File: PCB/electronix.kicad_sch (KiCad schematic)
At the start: 96 parts, among them IC1 ICM-20602, IC2 AP9101CK6-ANTRG1, IC3 DRV8210DRLR, IC4 DRV8210DRLR, J1 USB-C 6pin, J2 PRG, M1 N20 motor, M2 N20 motor, Q1 UMH3N FHA, Q2 757-SSM6N7002KFULF, Q3 757-SSM6N7002KFULF, Q4 Phototransistor, Q5 Phototransistor, Q6 757-SSM6N7002KFULF, Q7 Phototransistor, Q8 Phototransistor, SW1 SW_DIP_x01, SW2 RESET, SW3 START, U1 MCP73213-A6SI/MF, U2 ESP32-WROOM-32, U3 LMR51420YDDRCR

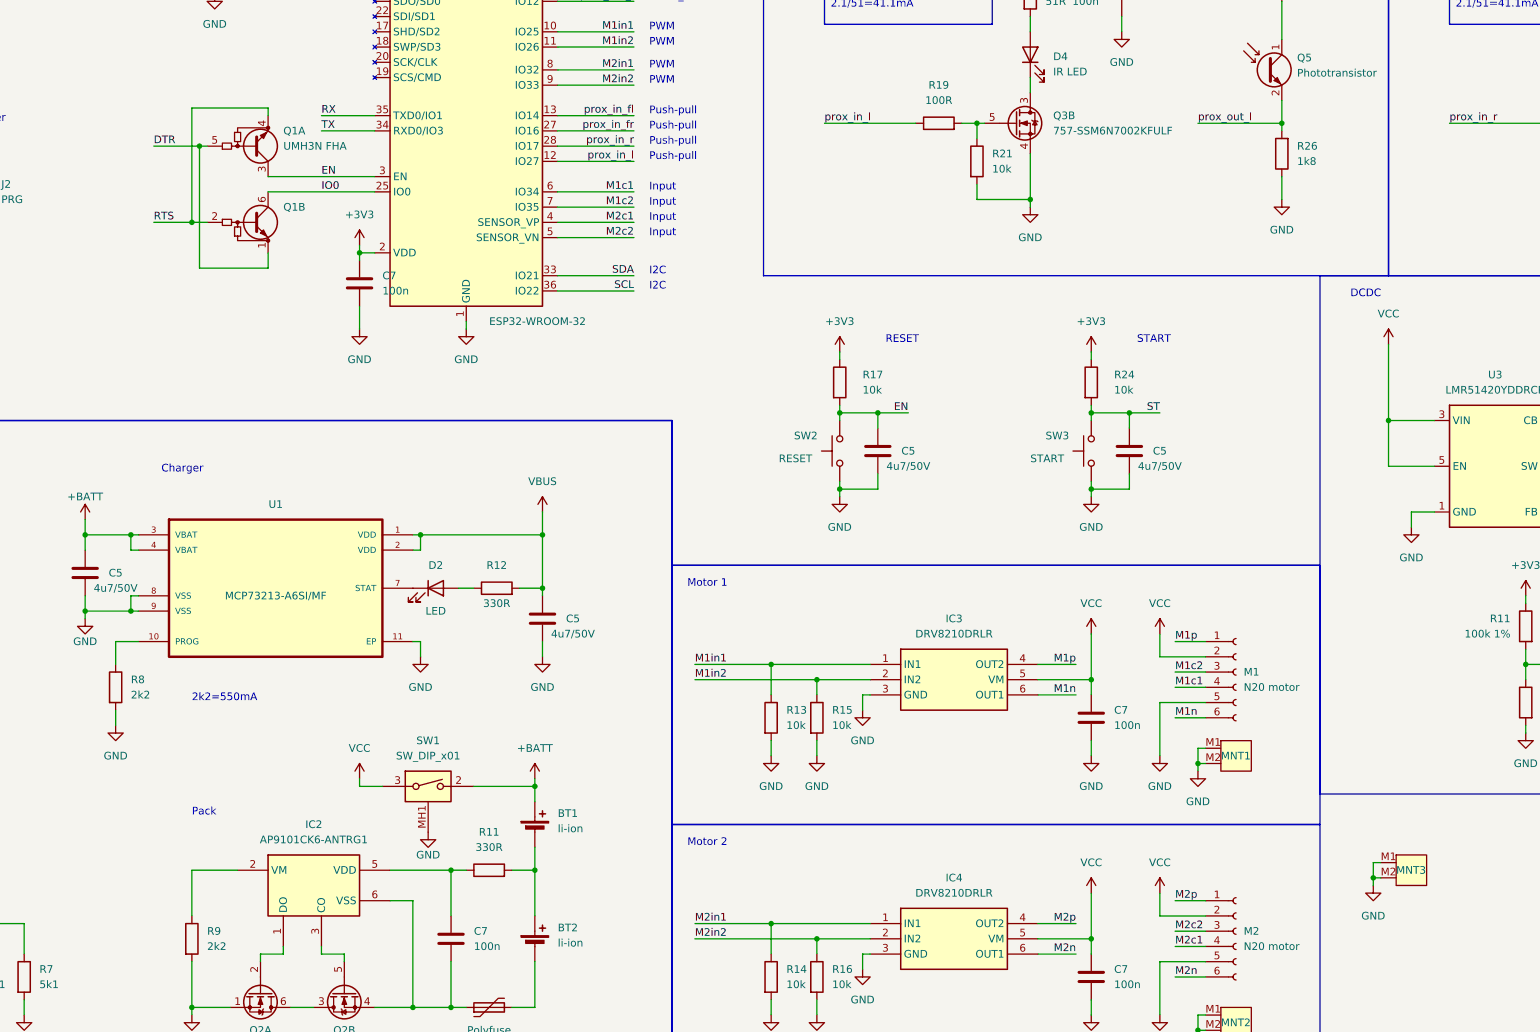
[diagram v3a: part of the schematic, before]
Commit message: add bigger ESP32 bypass
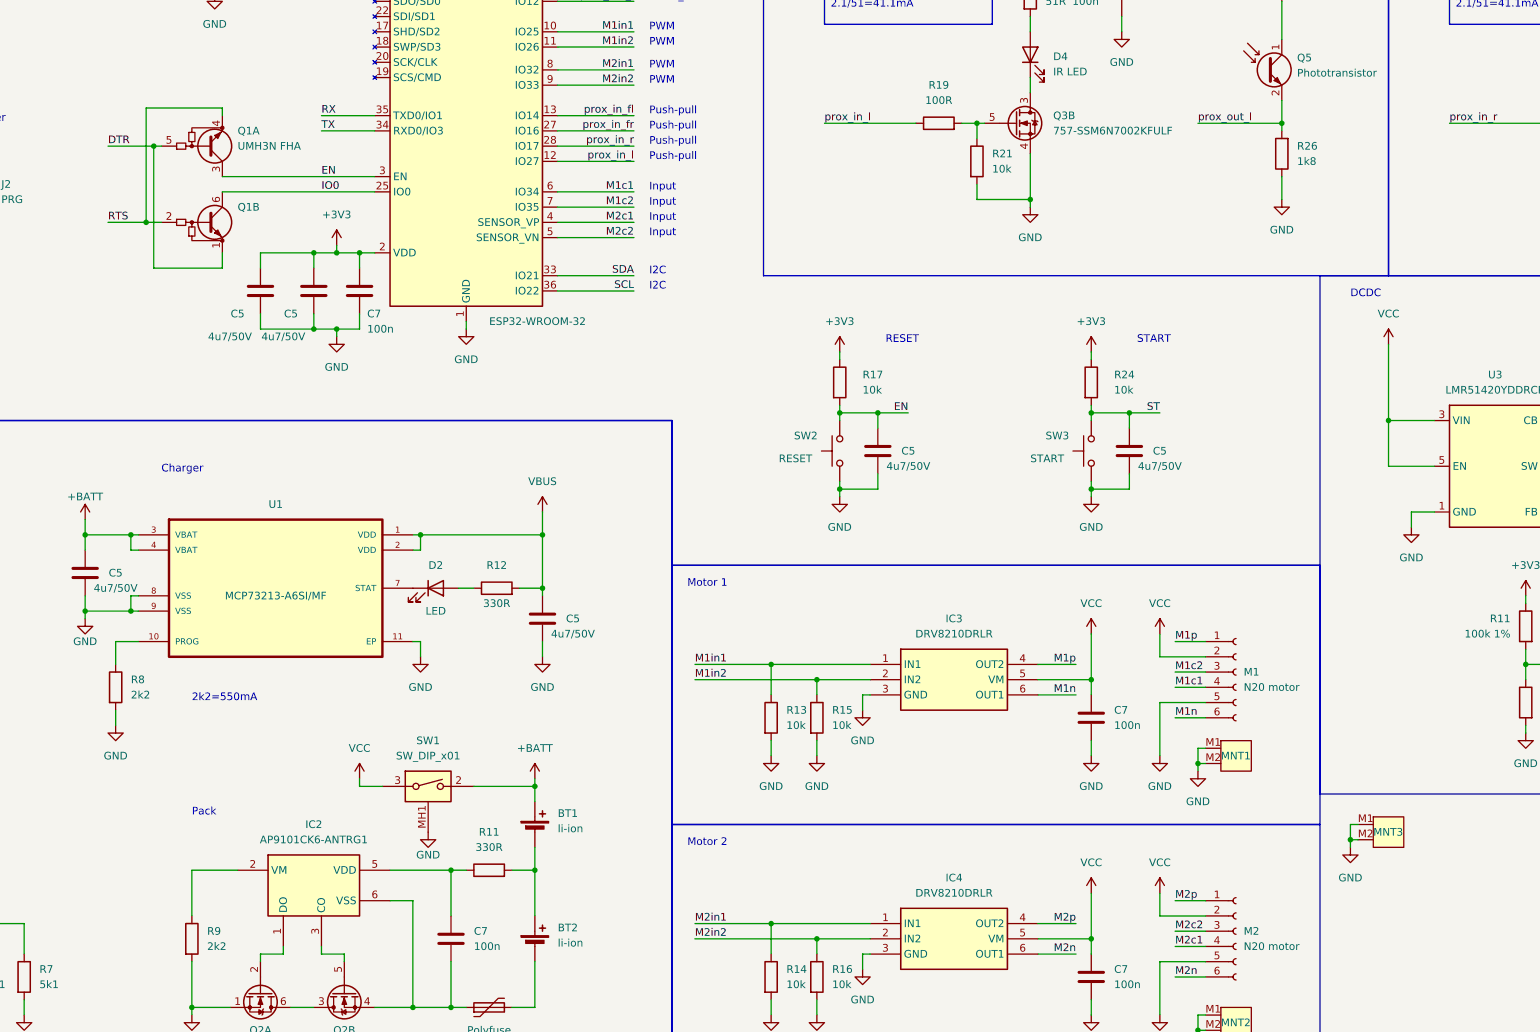
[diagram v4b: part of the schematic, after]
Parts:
- added C5 (x2): 4u7/50V, Capacitor_SMD:C_0805_2012Metric, symbol Device:C
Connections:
- net +3V3: now also C5.1, C5.1
- net GND: now also C5.2, C5.2
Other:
- moved on the sheet: C7, MNT3, Q1A, Q1B

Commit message: Add power source switching Add Mouser PN to parts to enable BOM generation Moved PWR indicator to side of board
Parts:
- removed D1: D, Diode_SMD:D_SOD-128, symbol Device:D
- removed D8: LED, LED_SMD:LED_0603_1608Metric, symbol Device:LED
- removed R37: 330R, Resistor_SMD:R_0603_1608Metric, symbol Device:R
- added D5: LED, LED_SMD:LED_0603_1608Metric, symbol Device:LED
- added IC5: LM66200DRLR, Package_TO_SOT_SMD:SOT-583-8, symbol LM66200DRLR:LM66200DRLR
- added R15: 10k, Resistor_SMD:R_0603_1608Metric, symbol Device:R
- added R26: 330R, Resistor_SMD:R_0603_1608Metric, symbol Device:R
- C5: Mouser Part Number (none) -> 81-GRM21BZ71H475ME5K
- C7: Mouser Part Number (none) -> 187-CL10B104KB8NNNC
- C7: value 100n/50V -> 100n; Mouser Part Number (none) -> 187-CL10B104KB8NNNC
- D1, D2: Mouser Part Number (none) -> 710-150060AS75000
- F1: Mouser Part Number (none) -> 576-1812L150/16DR
- IC1: Manufacturer_Name TDK -> (none); Manufacturer_Part_Number ICM-20602 -> (none); Mouser Price/Stock https://www.mouser.co.uk/ProductDetail/TDK-InvenSense/ICM-2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 -> (none)
- IC2: Height 1.4 -> (none); Manufacturer_Name Diodes Inc. -> (none); Manufacturer_Part_Number AP9101CK6-ANTRG1 -> (none); Mouser Price/Stock https://www.mouser.co.uk/ProductDetail/Diodes-Incorporated/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 -> (none)
- IC3, IC4: Height 0.6 -> (none); Manufacturer_Name Texas Instruments -> (none); Manufacturer_Part_Number DRV8210DRLR -> (none); Mouser Price/Stock https://www.mouser.co.uk/ProductDetail/Texas-Instruments/DR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 -> (none)
- J1: Mouser Part Number (none) -> 649-10164359-00011LF
- J2: Mouser Part Number (none) -> 992-6FX1L-254MM
- L1: Mouser Part Number (none) -> 963-NRS5040T3R3NMGJ
- Q1: Mouser Part Number (none) -> 755-UMH3NFHATN
- Q2, Q3, Q6: value 757-SSM6N7002KFULF -> dual NMOS; Mouser Part Number (none) -> 757-SSM6N7002KFULF
- R1, R4, R5: Mouser Part Number (none) -> 667-ERJ-3EKF1002V
- R10: Mouser Part Number (none) -> 791-RMC1/16-331JTP
- R11: Mouser Part Number (none) -> 603-RC0603FR-10100KL
- R11: renamed from R17; Mouser Part Number (none) -> 667-ERJ-3EKF1002V
- R12: renamed from R11; Mouser Part Number (none) -> 791-RMC1/16-331JTP
- R12: Mouser Part Number (none) -> 708-RMCF0603FT22K1
- R13: renamed from R12; Mouser Part Number (none) -> 791-RMC1/16-331JTP
- R14: renamed from R24; Mouser Part Number (none) -> 667-ERJ-3EKF1002V
- R16: renamed from R13; Mouser Part Number (none) -> 667-ERJ-3EKF1002V
- R17: renamed from R14; Mouser Part Number (none) -> 667-ERJ-3EKF1002V
- R18: renamed from R15; Mouser Part Number (none) -> 667-ERJ-3EKF1002V
- R19: renamed from R16; Mouser Part Number (none) -> 667-ERJ-3EKF1002V
- R20: renamed from R18; Mouser Part Number (none) -> 756-WCR0603-100RFI
- R21: renamed from R19; Mouser Part Number (none) -> 756-WCR0603-100RFI
- R22: renamed from R20; Mouser Part Number (none) -> 667-ERJ-3EKF1002V
- R23: renamed from R21; Mouser Part Number (none) -> 667-ERJ-3EKF1002V
- R24: renamed from R22; Mouser Part Number (none) -> 667-ERJ-PA3J510V
- R25: renamed from R23; Mouser Part Number (none) -> 667-ERJ-PA3J510V
- R27: renamed from R25; Mouser Part Number (none) -> 603-RC0603JR-071K8L
- R28: renamed from R26; Mouser Part Number (none) -> 603-RC0603JR-071K8L
- R31: renamed from R29; Mouser Part Number (none) -> 756-WCR0603-100RFI
- R32: renamed from R30; Mouser Part Number (none) -> 756-WCR0603-100RFI
- R33: renamed from R31; Mouser Part Number (none) -> 667-ERJ-3EKF1002V
- R34: renamed from R32; Mouser Part Number (none) -> 667-ERJ-3EKF1002V
- R35: renamed from R33; Mouser Part Number (none) -> 667-ERJ-PA3J510V
- R36: renamed from R34; Mouser Part Number (none) -> 667-ERJ-PA3J510V
- R37: renamed from R35; Mouser Part Number (none) -> 603-RC0603JR-071K8L
- R38: renamed from R36; Mouser Part Number (none) -> 603-RC0603JR-071K8L
- R6, R7: Mouser Part Number (none) -> 301-5.1K-RC
- R8, R9: Mouser Part Number (none) -> 660-RK73B1JTTD222J
- SW1: value SW_DIP_x01 -> side slide; Mouser Part Number (none) -> 655-1825232-1
- SW2, SW3: Mouser Part Number (none) -> 611-PTS636SL50LFS
- U1: AVAILABILITY Good -> (none); DESCRIPTION MCP Series 16V Dual-Cell Li-Ion/Li-Polymer Battery Charge M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 -> (none); MF Microchip -> (none); MP MCP73213-A6SI/MF -> (none); Mouser Part Number (none) -> 579-MCP73213-A6SI/MF; PACKAGE DFN-10 Microchip -> (none); PRICE 1.60 USD -> (none); SNAPEDA_PACKAGE_ID 30778 -> (none)
- U2: Mouser Part Number (none) -> 356-ESP32WRM32E132PH
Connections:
- net +3V3: now also D5.2 (A), IC5.2 (VOUT), IC5.7 (VOUT); no longer C5.1, C5.1, C5.1, L1.2, R11.1
- net GND: now also IC5.1 (GND), IC5.4 (~{ON}), IC5.5 (GND), R26.1
- net 3V3_PRG: now reaches J2.6 (Pin_6)
- net 3V3_PRG: now also IC5.6 (VIN2)
- new net: D5.1 (K), R26.2
- new net: IC5.8 (ST), R15.2
- new net 3V3_SW: C5.1, C5.1, C5.1, IC5.3 (VIN1), L1.2, R11.1, R15.1
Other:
- note added: "Power Switching"
- moved on the sheet: C5, R11, R14, SW2, SW3

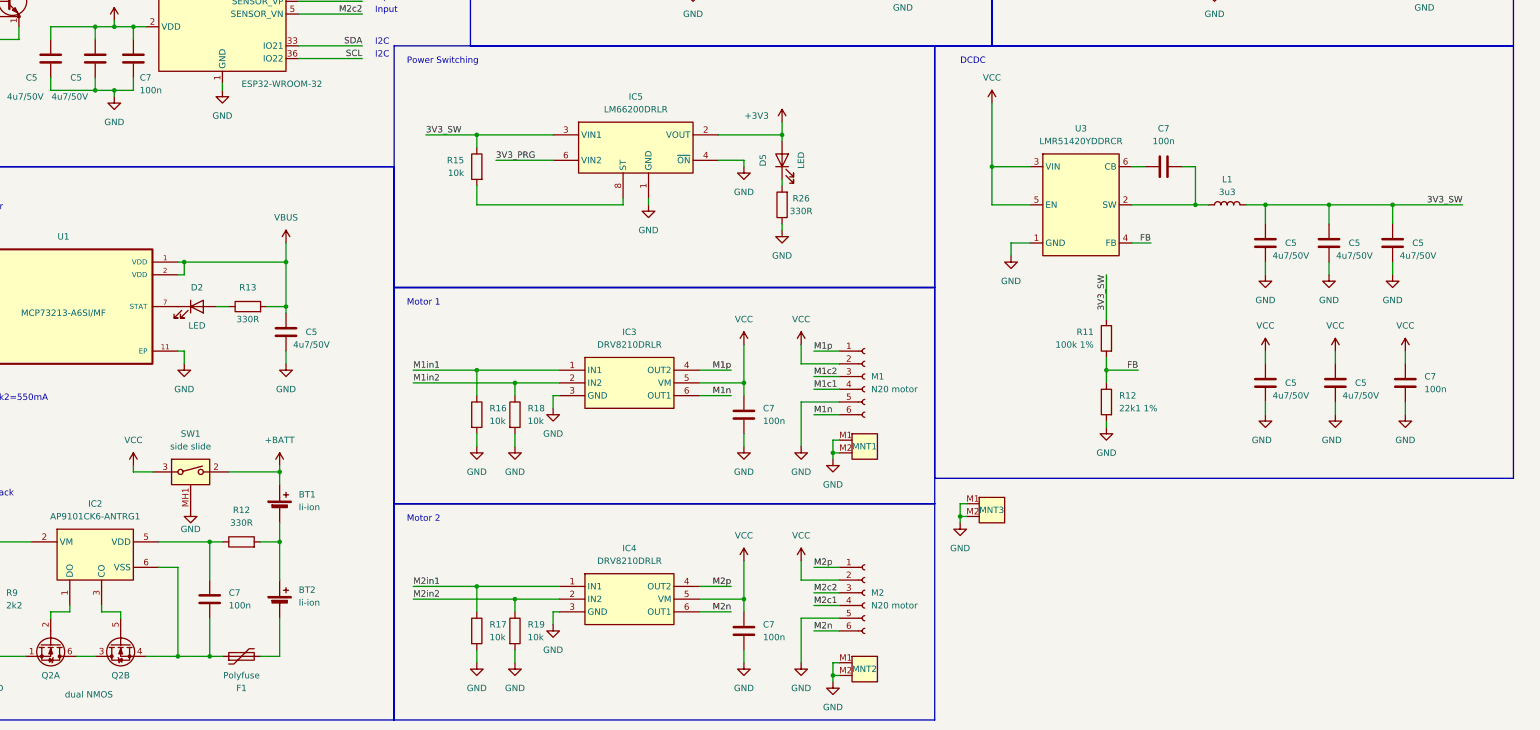
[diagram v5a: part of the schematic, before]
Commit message: Finishing touches shorten ground plane cuts fillet polygon pours add test points and PSU bringup jumper differentiate capacitor footprints by silkscreen
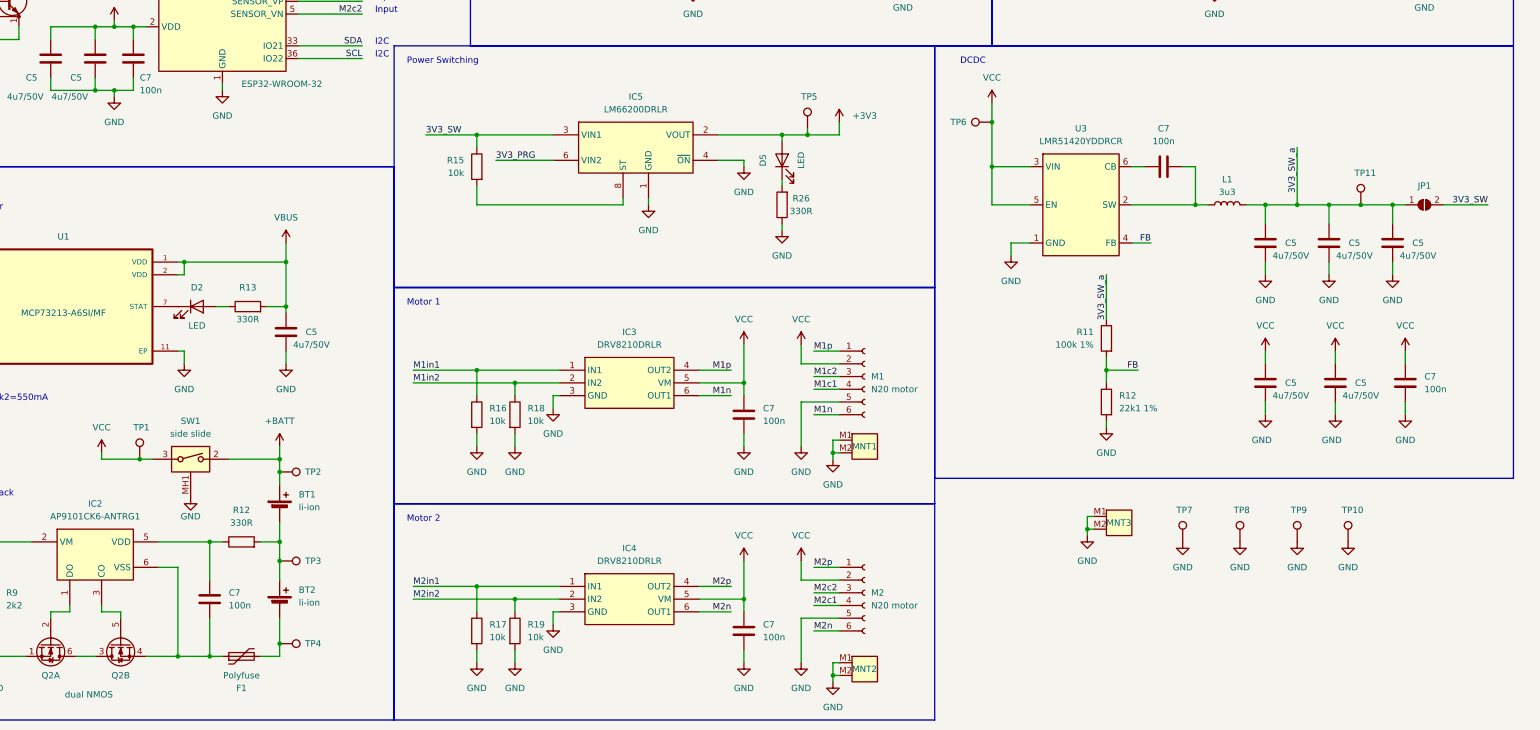
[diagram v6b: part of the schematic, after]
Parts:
- added JP1: SolderJumper_2_Open, Jumper:SolderJumper-2_P1.3mm_Open_TrianglePad1.0x1.5mm, symbol Jumper:SolderJumper_2_Open
- added TP1, TP10, TP11, TP2, TP3, TP4, TP5, TP6, TP7, TP8, TP9: TestPoint, TestPoint:TestPoint_Pad_1.0x1.0mm, symbol Connector:TestPoint
- C5: footprint Capacitor_SMD:C_0805_2012Metric -> Custom_parts:C_0805_2012Metric
- C7: footprint Capacitor_SMD:C_0603_1608Metric -> Custom_parts:C_0603_1608Metric
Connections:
- net +3V3: now also TP5.1
- net +BATT: now also TP2.1
- net 3V3_SW: now also JP1.2 (B); no longer C5.1, C5.1, C5.1, L1.2, R11.1
- net GND: now also TP10.1, TP7.1, TP8.1, TP9.1
- net VCC: now also TP1.1, TP6.1
- net at BT1.2 (-), BT2.1 (+), R12.2: now also TP3.1
- net at BT2.2 (-), F1.2: now also TP4.1
- new net 3V3_SW_a: C5.1, C5.1, C5.1, JP1.1 (A), L1.2, R11.1, TP11.1
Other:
- moved on the sheet: MNT3, SW1

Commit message: ESD hardening
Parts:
- added D1, D11, D12, D13, D14, D2, D3, D6, D7: PESD5V2S2UT, Package_TO_SOT_SMD:SOT-23-3, symbol Device:D_Dual_CommonAnode_KKA_Parallel
- added R2, R3, R30, R31, R32, R33, R35, R36, R4, R47, R48, R5: 100R, Resistor_SMD:R_0603_1608Metric, symbol Device:R
- M1, M2: value N20 motor -> N20
- renumbered D5 to D10, D6 to D15, D7 to D16, D1 to D4, D2 to D5, D3 to D8, D4 to D9, R6 to R10, R7 to R11, R8 to R12, R9 to R13, R10 to R14, R11 to R15, R12 to R16, R13 to R17, R14 to R18, R16 to R19, R17 to R20, R15 to R21, R18 to R22, R19 to R23, R20 to R24, R21 to R25, R22 to R26, R23 to R27, R24 to R28, R25 to R29, R26 to R34, R27 to R37, R28 to R38, R31 to R41, R32 to R42, R33 to R43, R34 to R44, R35 to R45, R36 to R46, R37 to R49, R38 to R50, R4 to R8, R5 to R9
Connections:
- net +BATT: now also D6.2 (K)
- net 3V3_PRG: now also D1.2 (K)
- net DTR: now also R3.1; no longer J2.2 (Pin_2)
- net GND: now also R19.1, D1.1 (K), D11.3 (A), D12.3 (A), D13.3 (A), D14.3 (A), D2.1 (K), D3.1 (K); no longer R19.2
- net M1c1: now also R31.1; no longer M1.4 (Pin_4)
- net M1c2: now also R30.1; no longer M1.3 (Pin_3)
- net M1in1: now also R19.2; no longer R19.1
- net M1n: now also D12.2 (K)
- net M1p: now also D11.1 (K)
- net M2c1: now also R33.1; no longer M2.4 (Pin_4)
- net M2c2: now also R32.1; no longer M2.3 (Pin_3)
- net M2n: now also D14.2 (K)
- net M2p: now also D13.1 (K)
- net RTS: now also R2.1; no longer J2.1 (Pin_1)
- net RX: now also R4.1; no longer J2.3 (Pin_3)
- net TX: now also R5.1; no longer J2.4 (Pin_4)
- net VBUS: now also D3.2 (K)
- net VCC: now also D2.2 (K)
- net prox_out_fl: now also R36.1; no longer Q4.2 (E), R37.2
- net prox_out_fr: now also R47.1; no longer Q7.2 (E), R49.2
- net prox_out_l: now also R35.1; no longer Q5.2 (E), R38.2
- net prox_out_r: now also R48.1; no longer Q8.2 (E), R50.2
- net at BT1.2 (-), BT2.1 (+), R16.2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: now also D6.1 (K), D7.2 (K)
- net at BT2.2 (-), F1.2, TP4.1: now also D7.1 (K)
- new net: J2.1 (Pin_1), R2.2
- new net: J2.2 (Pin_2), R3.2
- new net: J2.3 (Pin_3), R4.2
- new net: J2.4 (Pin_4), R5.2
- new net: Q4.2 (E), R36.2, R37.2
- new net: D13.2 (K), M2.3 (Pin_3), R32.2
- new net: D11.2 (K), M1.3 (Pin_3), R30.2
- new net: D12.1 (K), M1.4 (Pin_4), R31.2
- new net: Q7.2 (E), R47.2, R49.2
- new net: D14.1 (K), M2.4 (Pin_4), R33.2
- new net: Q5.2 (E), R35.2, R38.2
- new net: Q8.2 (E), R48.2, R50.2
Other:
- moved on the sheet: BT1, BT2, C7, F1, IC2, IC3, IC4, M1, MNT1, Q2A, Q2B, R13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
